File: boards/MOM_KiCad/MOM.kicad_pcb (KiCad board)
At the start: 2 copper layers, 34 parts, among them J1 JST-PH, J2 USB_C_Receptacle_USB2.0, Q1 DMP2045U, SW1 SW_Push, SW2 SW_Push, U1 AP2112M-3.3, U2 MCP73831, U3 MAX17048G+T10, U4 ESP32-S3-MINI-1

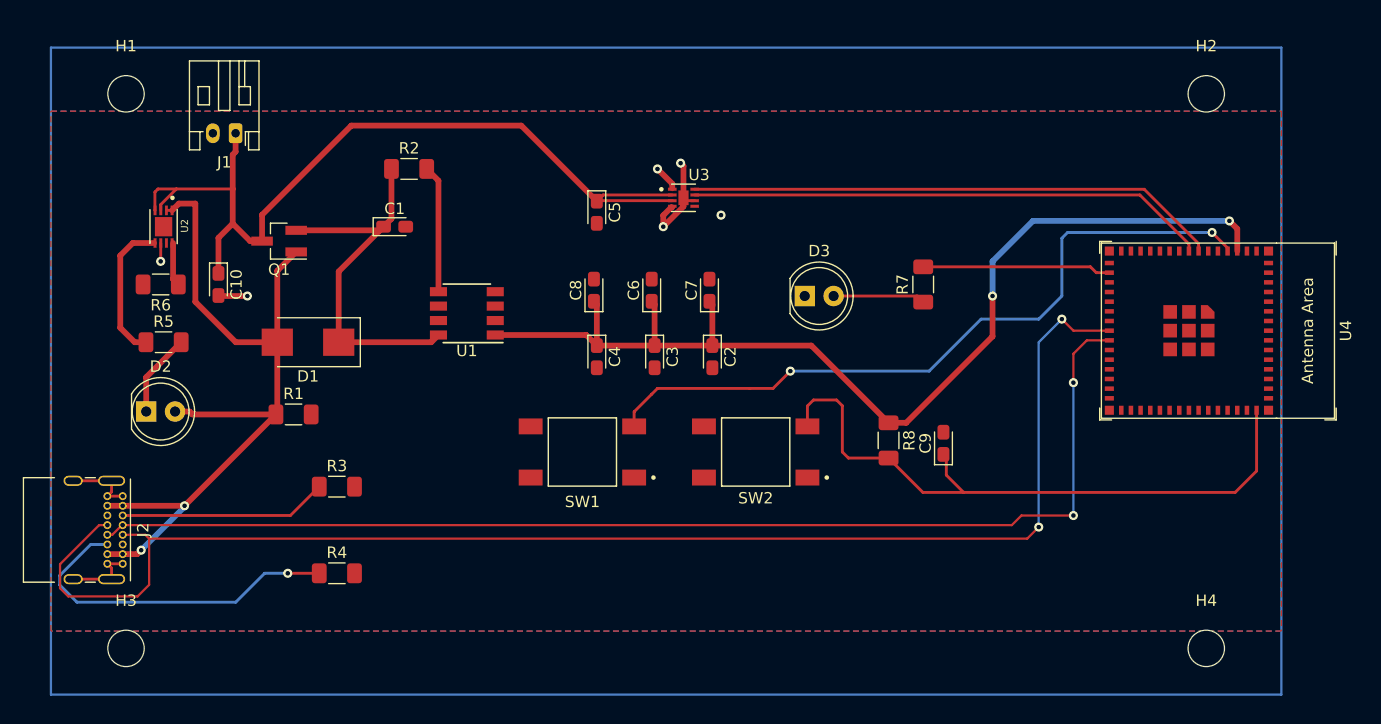
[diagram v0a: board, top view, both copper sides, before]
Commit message: Start POC code based off feather
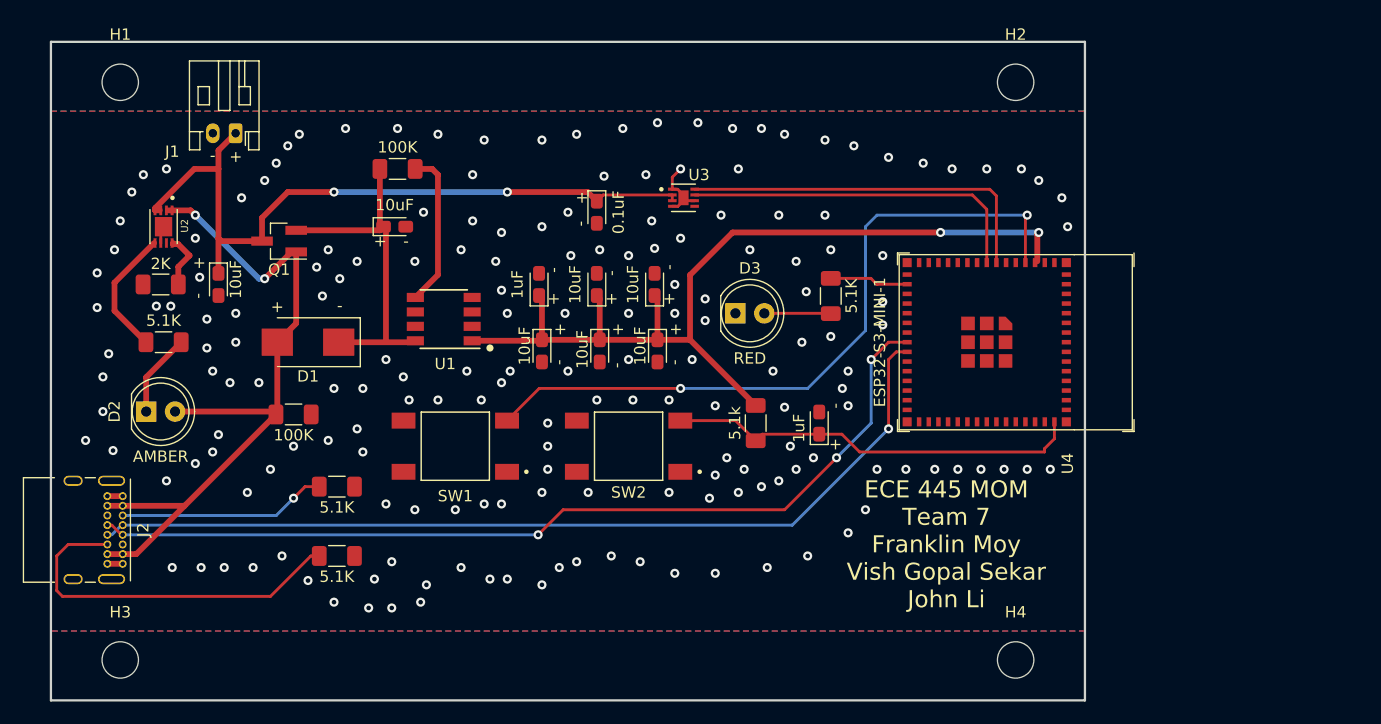
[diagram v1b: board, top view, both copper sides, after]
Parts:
- moved U4 17.8 mm to (152.4, 61.0)
- moved H2 16.8 mm to (154.9, 38.1)
- moved H4 16.8 mm to (154.9, 88.9)
- moved R8 11.8 mm to (132.1, 68.1)
- moved SW2 11.2 mm to (120.9, 70.1)
- moved SW1 11.2 mm to (105.7, 70.1)
- moved C9 11.1 mm to (137.7, 68.1)
- moved R7 8.19 mm to (138.7, 56.9)
- moved D3 6.28 mm to (130.3, 58.4)
- moved C2 4.85 mm to (123.4, 61.7)
- moved C6 4.85 mm to (118.1, 55.9)
- moved C3 4.85 mm to (118.4, 61.7)
- moved C4 4.85 mm to (113.3, 61.7)
- moved C7 4.85 mm to (123.2, 55.9)
- moved C8 4.85 mm to (113.0, 55.9)
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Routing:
- net /USB_D-: track 125.2 -> 80.9 mm, vias 2 -> 3
- net /USB_D+: track 103.5 -> 80.5 mm, vias 2 -> 1
- net /RESET: track 57.5 -> 36.7 mm
- net GND: track 28.5 -> 9.10 mm, vias 6 -> 182
- net +3.3V: track 93.9 -> 78.7 mm
- net /SCL: track 45.9 -> 30.9 mm
- net /SDA: track 46.9 -> 32.6 mm
- net +BATT: track 78.5 -> 64.6 mm, vias 0 -> 2
- net /GPIO13: track 16.6 -> 6.95 mm
- net VBUS: track 70.9 -> 64.5 mm
- net Net-(C1-Pad1): track 34.0 -> 29.6 mm
- net Net-(R2-Pad2): track 11.2 -> 13.8 mm
- net Net-(D3-Pad2): track 8.10 -> 5.82 mm
- net Net-(J2-PadB5): track 30.7 -> 32.7 mm, vias 1 -> 0
- net Net-(R5-Pad1): track 12.6 -> 11.3 mm
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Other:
- board outline added: 90.9 x 57.9 mm
- board text added: "ECE 445 MOM Team 7 Franklin Moy Vish Gopal Sekar John Li"
